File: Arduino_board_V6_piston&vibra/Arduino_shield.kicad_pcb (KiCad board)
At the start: 2 copper layers, 68.6 x 53.3 mm, 41 parts, among them J1 Conn_01x04_Male, J10 Conn_01x01_Male, J11 Conn_02x02_Odd_Even, J2 Conn_02x04_Odd_Even, J3 Conn_01x04_Male, J4 Conn_01x04_Male, J5 Conn_01x04_Male, J6 Conn_01x04_Male, J7 Conn_01x01_Male, J8 Conn_01x01_Male, J9 Conn_01x01_Male, Q1 Q_DUAL_NPN_NPN_BRT_E1B1C2E2B2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, Q2 Q_DUAL_NPN_NPN_BRT_E1B1C2E2B2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, U1 ARDUINOR3-DIMENSION

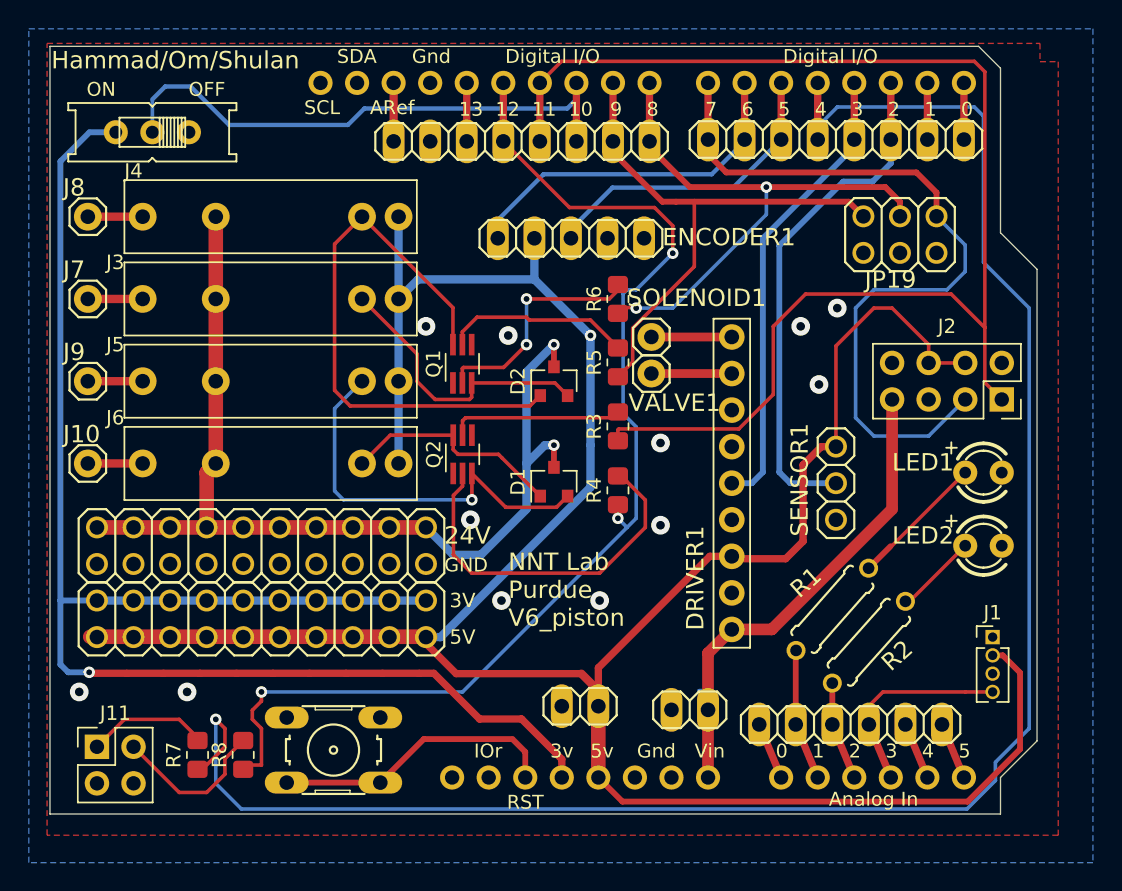
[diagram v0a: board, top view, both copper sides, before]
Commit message: change the arduino output
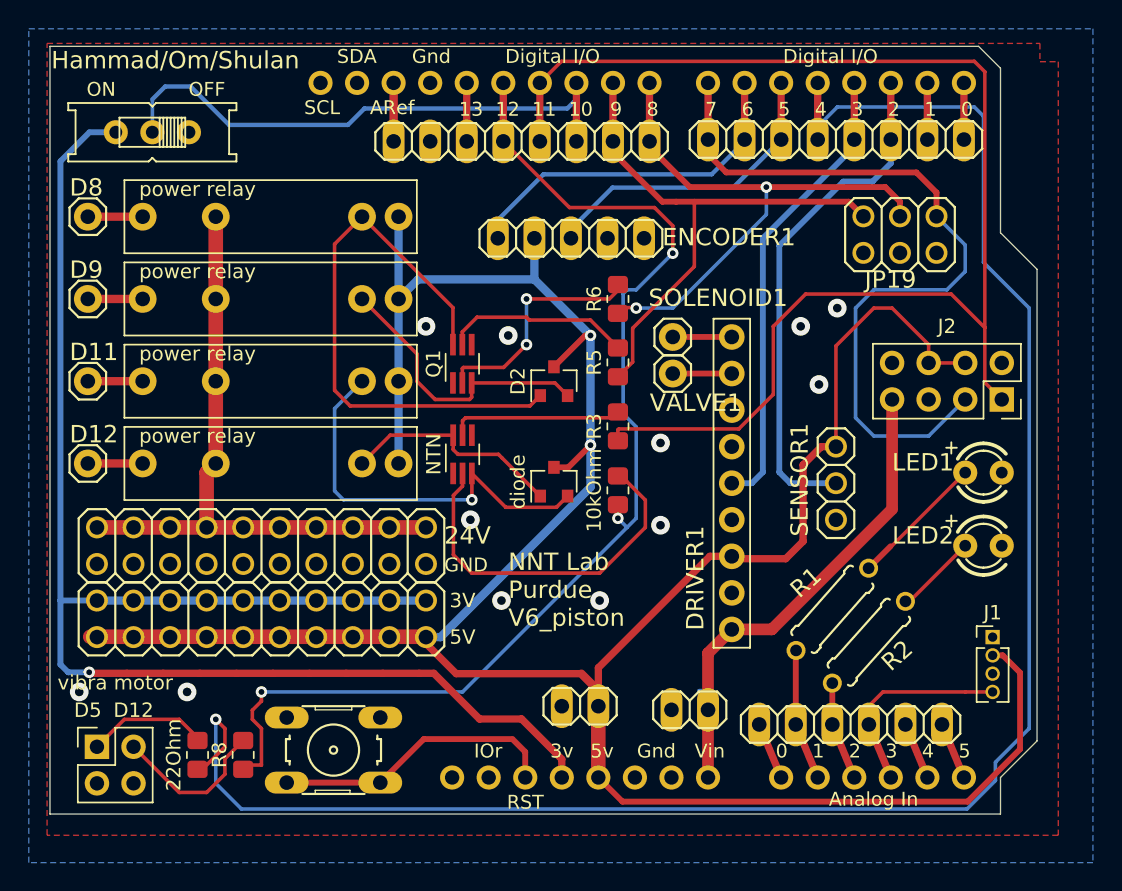
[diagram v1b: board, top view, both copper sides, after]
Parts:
- power relay: renamed from J4
- power relay: renamed from J5
- power relay: renamed from J6
- power relay: renamed from J3
- vibra motor: renamed from J11
- moved SOLENOID1 1.49 mm to (157.5, 98.5)
- moved VALVE1 1.49 mm to (157.5, 101.1)
- renumbered R4 to 10kOhm, R7 to 22Ohm, J9 to D11, J10 to D12, J8 to D8, J7 to D9, Q2 to NTN, D1 to diode
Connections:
- D2 pad 3: VDD_24V -> VCC
- diode pad 3: VDD_24V -> VCC
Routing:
- net VDD_24V: track 71.5 -> 44.7 mm, vias 2 -> 0
- net VCC: track 193.7 -> 200.3 mm, vias 1 -> 2
- net Net-(DRIVER1-Pad9): track 5.59 -> 4.10 mm
- net Net-(DRIVER1-Pad8): track 5.59 -> 4.10 mm
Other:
- board text added: "D12"
- board text added: "D5"
